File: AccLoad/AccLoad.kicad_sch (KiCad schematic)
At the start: 6 parts

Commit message: ...
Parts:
- added R6: 100 кОм*, symbol Device:R
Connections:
- net i1: now also R6.2
- net u1: now also R6.1
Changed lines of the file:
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@@
   (junction (at 63.5 59.69) (diameter 0) (color 0 0 0 0)
   )
+  (junction (at 105.41 43.18) (diameter 0) (color 0 0 0 0)
+  )
   (junction (at 63.5 64.77) (diameter 0) (color 0 0 0 0)
   )
+  (junction (at 105.41 50.8) (diameter 0) (color 0 0 0 0)
+  )
   (junction (at 87.63 50.8) (diameter 0) (color 0 0 0 0)
   )
@@
     (stroke (width 0) (type default) (color 0 0 0 0))
   )
+  (wire (pts (xy 101.6 43.18) (xy 105.41 43.18))
+    (stroke (width 0) (type default) (color 0 0 0 0))
+  )
   (wire (pts (xy 63.5 59.69) (xy 63.5 64.77))
     (stroke (width 0) (type default) (color 0 0 0 0))
@@
   )
   (wire (pts (xy 27.94 59.69) (xy 29.21 59.69))
+    (stroke (width 0) (type default) (color 0 0 0 0))
+  )
+  (wire (pts (xy 101.6 50.8) (xy 105.41 50.8))
     (stroke (width 0) (type default) (color 0 0 0 0))
   )
@@
     (pin "2")
   )
+  (symbol (lib_id "Device:R") (at 101.6 46.99 0) (unit 1)
+    (in_bom yes) (on_board yes)
+    (property "Reference" "R6" (id 0) (at 100.33 54.61 0)
+      (effects (font (size 1.27 1.27)) (justify left))
+    )
+    (property "Value" "100 кОм*" (id 1) (at 95.25 57.15 0)
+      (effects (font (size 1.27 1.27)) (justify left))
+    )
+    (property "Footprint" "" (id 2) (at 99.822 46.99 90)
+      (effects (font (size 1.27 1.27)) hide)
+    )
+    (property "Datasheet" "~" (id 3) (at 101.6 46.99 0)
+      (effects (font (size 1.27 1.27)) hide)
+    )
+    (pin "1")
+    (pin "2")
+  )
   (symbol (lib_id "power:GND") (at 63.5 69.85 0) (unit 1)
     (in_bom yes) (on_board yes) (fields_autoplaced)
@@
       (reference "R5") (unit 1) (value "1 кОм") (footprint "")
     )
-  )
+    (path "/81cea36f-374e-495b-8b76-6e2c7f3900a5"
+      (reference "R6") (unit 1) (value "100 кОм*") (footprint "")
+    )
+  )

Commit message: beta
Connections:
- net GND: now also R5.2, R6.2
- net i1: no longer R5.2, R6.2
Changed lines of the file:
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@@
   (junction (at 63.5 64.77) (diameter 0) (color 0 0 0 0)
-  )
-  (junction (at 105.41 50.8) (diameter 0) (color 0 0 0 0)
   )
   (junction (at 87.63 50.8) (diameter 0) (color 0 0 0 0)
@@
   (junction (at 87.63 59.69) (diameter 0) (color 0 0 0 0)
   )
+  (junction (at 105.41 50.8) (diameter 0) (color 0 0 0 0)
+  )
   (junction (at 83.82 41.91) (diameter 0) (color 0 0 0 0)
   )
   (junction (at 105.41 41.91) (diameter 0) (color 0 0 0 0)
   )
+  (junction (at 105.41 64.77) (diameter 0) (color 0 0 0 0)
+  )
   (junction (at 90.17 41.91) (diameter 0) (color 0 0 0 0)
   )
-  (junction (at 105.41 59.69) (diameter 0) (color 0 0 0 0)
-  )
-  (wire (pts (xy 63.5 64.77) (xy 118.11 64.77))
+  (wire (pts (xy 63.5 64.77) (xy 105.41 64.77))
     (stroke (width 0) (type default) (color 0 0 0 0))
   )
@@
     (stroke (width 0) (type default) (color 0 0 0 0))
   )
-  (wire (pts (xy 118.11 59.69) (xy 105.41 59.69))
+  (wire (pts (xy 87.63 59.69) (xy 118.11 59.69))
     (stroke (width 0) (type default) (color 0 0 0 0))
   )
   (wire (pts (xy 83.82 41.91) (xy 83.82 43.18))
+    (stroke (width 0) (type default) (color 0 0 0 0))
+  )
+  (wire (pts (xy 105.41 64.77) (xy 118.11 64.77))
     (stroke (width 0) (type default) (color 0 0 0 0))
   )
@@
   )
   (polyline (pts (xy 255.27 101.6) (xy 256.54 101.6))
-    (stroke (width 0) (type default) (color 0 0 0 0))
-  )
-  (wire (pts (xy 105.41 59.69) (xy 87.63 59.69))
     (stroke (width 0) (type default) (color 0 0 0 0))
   )
@@
     (stroke (width 0) (type default) (color 0 0 0 0))
   )
+  (wire (pts (xy 105.41 50.8) (xy 105.41 64.77))
+    (stroke (width 0) (type default) (color 0 0 0 0))
+  )
   (polyline (pts (xy 191.77 96.52) (xy 166.37 96.52))
     (stroke (width 0) (type default) (color 0 0 0 0))
@@
     (stroke (width 0) (type default) (color 0 0 0 0))
   )
-  (wire (pts (xy 105.41 50.8) (xy 105.41 59.69))
-    (stroke (width 0) (type default) (color 0 0 0 0))
-  )

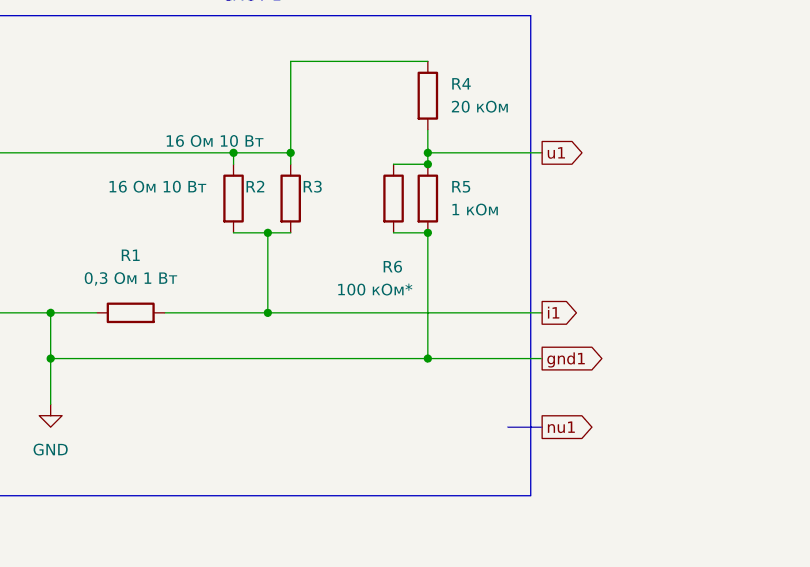
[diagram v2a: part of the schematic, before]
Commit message: added res to Ipin
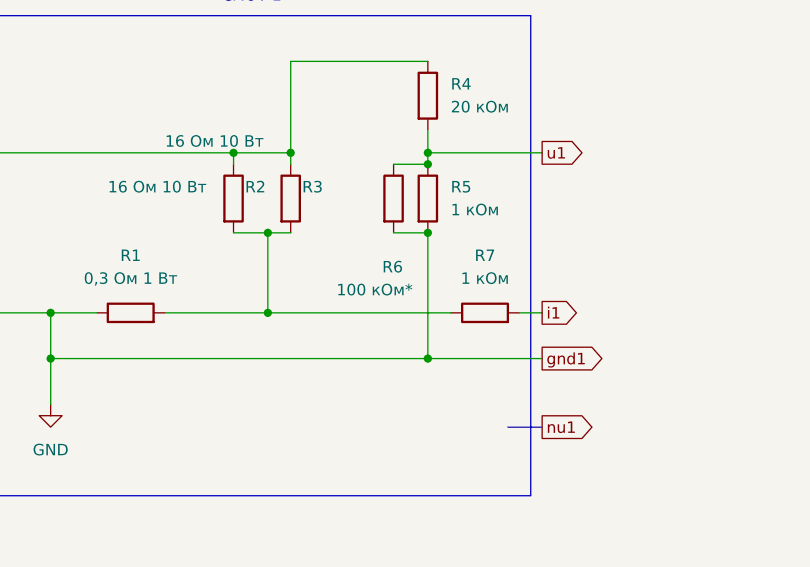
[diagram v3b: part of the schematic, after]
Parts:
- added R7: 1 кОм, symbol Device:R
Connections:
- net i1: now also R7.2; no longer R1.2, R2.2, R3.2
- new net: R1.2, R2.2, R3.2, R7.1
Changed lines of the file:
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@@
   (junction (at 87.63 50.8) (diameter 0) (color 0 0 0 0)
   )
+  (junction (at 105.41 50.8) (diameter 0) (color 0 0 0 0)
+  )
+  (junction (at 83.82 41.91) (diameter 0) (color 0 0 0 0)
+  )
+  (junction (at 105.41 41.91) (diameter 0) (color 0 0 0 0)
+  )
+  (junction (at 105.41 64.77) (diameter 0) (color 0 0 0 0)
+  )
+  (junction (at 90.17 41.91) (diameter 0) (color 0 0 0 0)
+  )
   (junction (at 87.63 59.69) (diameter 0) (color 0 0 0 0)
   )
-  (junction (at 105.41 50.8) (diameter 0) (color 0 0 0 0)
-  )
-  (junction (at 83.82 41.91) (diameter 0) (color 0 0 0 0)
-  )
-  (junction (at 105.41 41.91) (diameter 0) (color 0 0 0 0)
-  )
-  (junction (at 105.41 64.77) (diameter 0) (color 0 0 0 0)
-  )
-  (junction (at 90.17 41.91) (diameter 0) (color 0 0 0 0)
-  )
   (wire (pts (xy 63.5 64.77) (xy 105.41 64.77))
     (stroke (width 0) (type default) (color 0 0 0 0))
@@
     (stroke (width 0) (type default) (color 0 0 0 0))
   )
-  (wire (pts (xy 87.63 59.69) (xy 118.11 59.69))
-    (stroke (width 0) (type default) (color 0 0 0 0))
-  )
   (wire (pts (xy 83.82 41.91) (xy 83.82 43.18))
     (stroke (width 0) (type default) (color 0 0 0 0))
@@
     (stroke (width 0) (type default) (color 0 0 0 0))
   )
+  (wire (pts (xy 115.57 59.69) (xy 118.11 59.69))
+    (stroke (width 0) (type default) (color 0 0 0 0))
+  )
   (wire (pts (xy 87.63 50.8) (xy 90.17 50.8))
     (stroke (width 0) (type default) (color 0 0 0 0))
@@
   )
   (polyline (pts (xy 234.95 97.79) (xy 234.95 104.14))
+    (stroke (width 0) (type default) (color 0 0 0 0))
+  )
+  (wire (pts (xy 87.63 59.69) (xy 107.95 59.69))
     (stroke (width 0) (type default) (color 0 0 0 0))
   )
@@
     (effects (font (size 1.27 1.27)) (justify left))
   )
+  (symbol (lib_id "Device:R") (at 111.76 59.69 90) (unit 1)
+    (in_bom yes) (on_board yes) (fields_autoplaced)
+    (property "Reference" "R7" (id 0) (at 111.76 53.34 90))
+    (property "Value" "1 кОм" (id 1) (at 111.76 55.88 90))
+    (property "Footprint" "" (id 2) (at 111.76 61.468 90)
+      (effects (font (size 1.27 1.27)) hide)
+    )
+    (property "Datasheet" "~" (id 3) (at 111.76 59.69 0)
+      (effects (font (size 1.27 1.27)) hide)
+    )
+    (pin "1")
+    (pin "2")
+  )
   (symbol (lib_id "Device:R") (at 72.39 59.69 90) (unit 1)
     (in_bom yes) (on_board yes) (fields_autoplaced)
@@
       (reference "R6") (unit 1) (value "100 кОм*") (footprint "")
     )
-  )
+    (path "/581c5c8f-e5ca-4a65-84bc-e03c379cadc0"
+      (reference "R7") (unit 1) (value "1 кОм") (footprint "")
+    )
+  )

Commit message: star PCB designing
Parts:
- added H1: bat+, MountingHole:MountingHole_2.2mm_M2_DIN965_Pad_TopBottom, symbol Mechanical:MountingHole_Pad
- added H2: bat-, MountingHole:MountingHole_2.2mm_M2_DIN965_Pad_TopBottom, symbol Mechanical:MountingHole_Pad
- added H3: load+, MountingHole:MountingHole_2.2mm_M2_DIN965_Pad_TopBottom, symbol Mechanical:MountingHole_Pad
- added H4: load-, MountingHole:MountingHole_2.2mm_M2_DIN965_Pad_TopBottom, symbol Mechanical:MountingHole_Pad
- added J1: to MCU, Connector_JST:JST_EH_B4B-EH-A_1x04_P2.50mm_Vertical, symbol Connector:Conn_01x04_Male
- added R1, R2: 1 Ом 1 Вт, Resistor_SMD:R_2512_6332Metric_Pad1.40x3.35mm_HandSolder, symbol Device:R
- added R6, R7, R8: 6,8 Ом 10 Вт, symbol Device:R
- BT1: now left out of the parts list
- R10: renamed from R4; footprint (none) -> Resistor_SMD:R_0805_2012Metric_Pad1.20x1.40mm_HandSolder
- R11: renamed from R5; footprint (none) -> Resistor_SMD:R_0805_2012Metric_Pad1.20x1.40mm_HandSolder
- R12: renamed from R7; footprint (none) -> Resistor_SMD:R_0805_2012Metric_Pad1.20x1.40mm_HandSolder
- R3: value 16 Ом 10 Вт -> 1 Ом 1 Вт; footprint (none) -> Resistor_SMD:R_2512_6332Metric_Pad1.40x3.35mm_HandSolder
- R4: renamed from R1; value 0,3 Ом 1 Вт -> 1 Ом 1 Вт; footprint (none) -> Resistor_SMD:R_2512_6332Metric_Pad1.40x3.35mm_HandSolder
- R5: renamed from R2; value 16 Ом 10 Вт -> 6,8 Ом 10 Вт; now left out of the parts list
- R9: renamed from R6; footprint (none) -> Resistor_SMD:R_0805_2012Metric_Pad1.20x1.40mm_HandSolder
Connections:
- net GND: now also R3.1, H2.1, J1.3 (Pin_3), R1.1, R2.1
- net bat1+: now also H1.1, H3.1, R7.1; no longer R3.1
- net i1: now also J1.2 (Pin_2)
- net u1: now also J1.4 (Pin_4)
- net at R12.1, R3.2, R4.2: now also H4.1, R1.2, R2.2, R6.2, R8.2; no longer R5.2
- new net: R5.2, R6.1, R7.2, R8.1
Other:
- moved on the sheet: R10, R11, R12, R4, R5, R9

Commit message: changed b2b
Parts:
- J1: footprint Connector_JST:JST_EH_B4B-EH-A_1x04_P2.50mm_Vertical -> Connector_JST:JST_PH_B4B-PH-K_1x04_P2.00mm_Vertical
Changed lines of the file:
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@@
       (effects (font (size 1.27 1.27)) (justify right))
     )
-    (property "Footprint" "Connector_JST:JST_EH_B4B-EH-A_1x04_P2.50mm_Vertical" (id 2) (at 161.29 55.88 0)
+    (property "Footprint" "Connector_JST:JST_PH_B4B-PH-K_1x04_P2.00mm_Vertical" (id 2) (at 161.29 55.88 0)
       (effects (font (size 1.27 1.27)) hide)
     )
@@
     )
     (path "/2a292674-a08c-4161-8921-c6c48539d8a7"
-      (reference "J1") (unit 1) (value "to MCU") (footprint "Connector_JST:JST_EH_B4B-EH-A_1x04_P2.50mm_Vertical")
+      (reference "J1") (unit 1) (value "to MCU") (footprint "Connector_JST:JST_PH_B4B-PH-K_1x04_P2.00mm_Vertical")
     )
     (path "/73eb8cce-d31f-424a-b1d5-e63d534c181c"

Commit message: fixed errors
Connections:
- net i1: now also J1.1 (Pin_1); no longer J1.2 (Pin_2)
- net u1: now also J1.2 (Pin_2); no longer J1.4 (Pin_4)
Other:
- moved on the sheet: J1

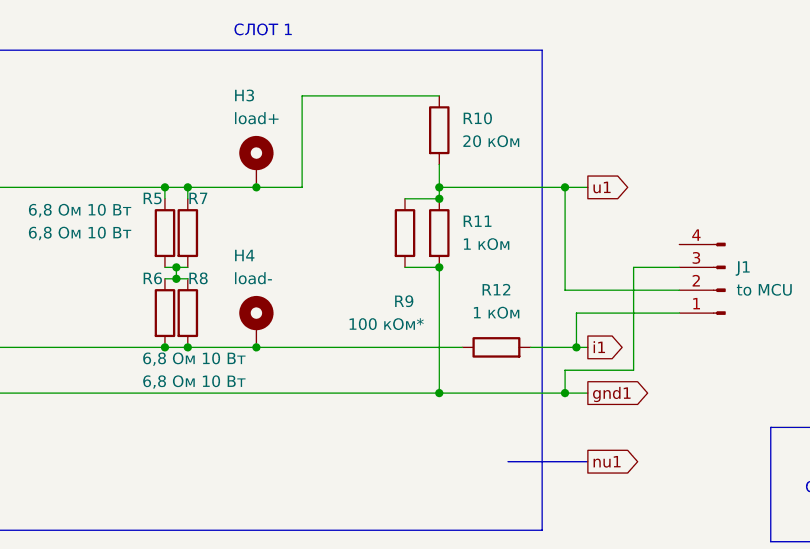
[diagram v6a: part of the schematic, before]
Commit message: PCD maked
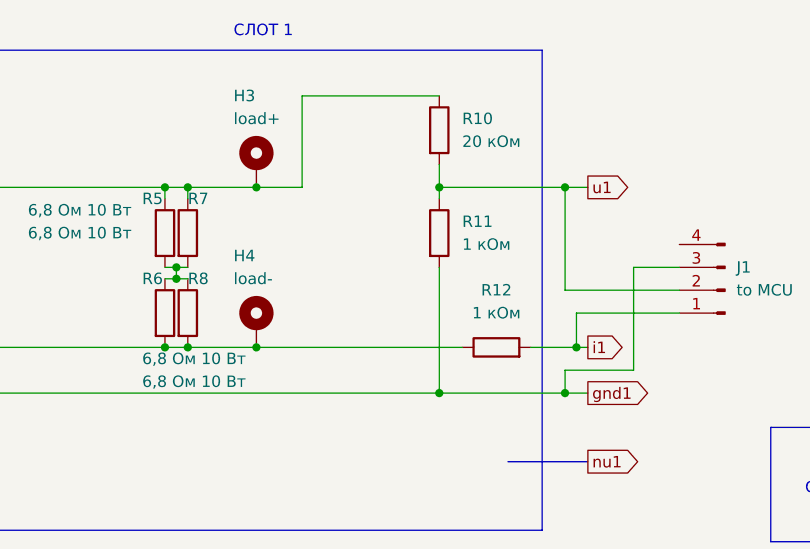
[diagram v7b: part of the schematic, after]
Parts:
- removed R9: 100 кОм*, Resistor_SMD:R_0805_2012Metric_Pad1.20x1.40mm_HandSolder, symbol Device:R
- H1, H2: footprint MountingHole:MountingHole_2.2mm_M2_DIN965_Pad_TopBottom -> Connector_Wire:SolderWire-1.5sqmm_1x01_D1.7mm_OD3.9mm
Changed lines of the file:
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@@
   (junction (at 63.5 59.69) (diameter 0) (color 0 0 0 0)
   )
-  (junction (at 129.54 43.18) (diameter 0) (color 0 0 0 0)
-  )
   (junction (at 143.51 64.77) (diameter 0) (color 0 0 0 0)
   )
@@
   (junction (at 144.78 59.69) (diameter 0) (color 0 0 0 0)
   )
-  (junction (at 129.54 50.8) (diameter 0) (color 0 0 0 0)
-  )
   (junction (at 99.06 41.91) (diameter 0) (color 0 0 0 0)
   )
@@
     (stroke (width 0) (type default) (color 0 0 0 0))
   )
-  (wire (pts (xy 125.73 43.18) (xy 129.54 43.18))
-    (stroke (width 0) (type default) (color 0 0 0 0))
-  )
   (wire (pts (xy 63.5 59.69) (xy 63.5 64.77))
     (stroke (width 0) (type default) (color 0 0 0 0))
@@
   )
   (wire (pts (xy 100.33 50.8) (xy 101.6 50.8))
-    (stroke (width 0) (type default) (color 0 0 0 0))
-  )
-  (wire (pts (xy 125.73 50.8) (xy 129.54 50.8))
     (stroke (width 0) (type default) (color 0 0 0 0))
   )
@@
       (effects (font (size 1.27 1.27)) (justify left))
     )
-    (property "Footprint" "MountingHole:MountingHole_2.2mm_M2_DIN965_Pad_TopBottom" (id 2) (at 53.34 57.15 0)
+    (property "Footprint" "Connector_Wire:SolderWire-1.5sqmm_1x01_D1.7mm_OD3.9mm" (id 2) (at 53.34 57.15 0)
       (effects (font (size 1.27 1.27)) hide)
     )
@@
     (pin "1")
   )
-  (symbol (lib_id "Device:R") (at 125.73 46.99 0) (unit 1)
-    (in_bom yes) (on_board yes)
-    (property "Reference" "R9" (id 0) (at 124.46 54.61 0)
-      (effects (font (size 1.27 1.27)) (justify left))
-    )
-    (property "Value" "100 кОм*" (id 1) (at 119.38 57.15 0)
-      (effects (font (size 1.27 1.27)) (justify left))
-    )
-    (property "Footprint" "Resistor_SMD:R_0805_2012Metric_Pad1.20x1.40mm_HandSolder" (id 2) (at 123.952 46.99 90)
-      (effects (font (size 1.27 1.27)) hide)
-    )
-    (property "Datasheet" "~" (id 3) (at 125.73 46.99 0)
-      (effects (font (size 1.27 1.27)) hide)
-    )
-    (pin "1")
-    (pin "2")
-  )
   (symbol (lib_id "Mechanical:MountingHole_Pad") (at 53.34 39.37 0) (unit 1)
     (in_bom yes) (on_board yes)
@@
       (effects (font (size 1.27 1.27)) (justify left))
     )
-    (property "Footprint" "MountingHole:MountingHole_2.2mm_M2_DIN965_Pad_TopBottom" (id 2) (at 53.34 39.37 0)
+    (property "Footprint" "Connector_Wire:SolderWire-1.5sqmm_1x01_D1.7mm_OD3.9mm" (id 2) (at 53.34 39.37 0)
       (effects (font (size 1.27 1.27)) hide)
     )
@@
     )
     (path "/9a6e80bf-c796-4efa-8466-bb1e955a96d0"
-      (reference "H1") (unit 1) (value "bat+") (footprint "MountingHole:MountingHole_2.2mm_M2_DIN965_Pad_TopBottom")
+      (reference "H1") (unit 1) (value "bat+") (footprint "Connector_Wire:SolderWire-1.5sqmm_1x01_D1.7mm_OD3.9mm")
     )
     (path "/6721b285-34e3-48c4-b169-d24d9cdc7908"
-      (reference "H2") (unit 1) (value "bat-") (footprint "MountingHole:MountingHole_2.2mm_M2_DIN965_Pad_TopBottom")
+      (reference "H2") (unit 1) (value "bat-") (footprint "Connector_Wire:SolderWire-1.5sqmm_1x01_D1.7mm_OD3.9mm")
     )
     (path "/a4d0027d-002d-4e39-bf71-8479da179a54"
@@
       (reference "R8") (unit 1) (value "6,8 Ом 10 Вт") (footprint "")
     )
-    (path "/81cea36f-374e-495b-8b76-6e2c7f3900a5"
-      (reference "R9") (unit 1) (value "100 кОм*") (footprint "Resistor_SMD:R_0805_2012Metric_Pad1.20x1.40mm_HandSolder")
-    )
     (path "/f2f92b50-07ae-4197-8fc5-ea1dcb1dc123"

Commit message: fixed PCB error with voltmeter+- and border reroute
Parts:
- added H3: v+, Sharonov:APEX_voltmeter_pin, symbol Mechanical:MountingHole_Pad
- added H4: v-, Sharonov:APEX_voltmeter_pin, symbol Mechanical:MountingHole_Pad
- renumbered H3 to H5, H4 to H6, R11 to R10, R12 to R11, R10 to R9
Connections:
- net GND: now also H4.1
- net bat1+: now also H3.1
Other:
- moved on the sheet: BT1, H1, H2
